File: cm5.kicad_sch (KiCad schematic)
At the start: 0 parts

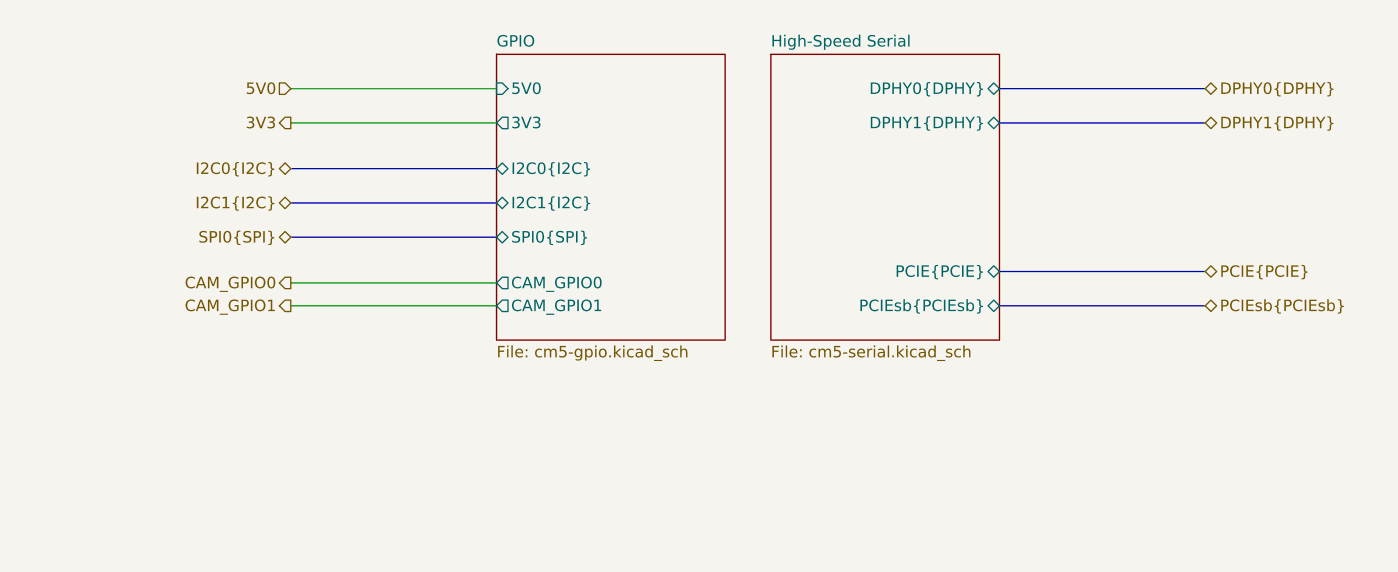
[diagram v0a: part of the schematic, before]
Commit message: prepared usb3, abstracted cameras, backplane connector
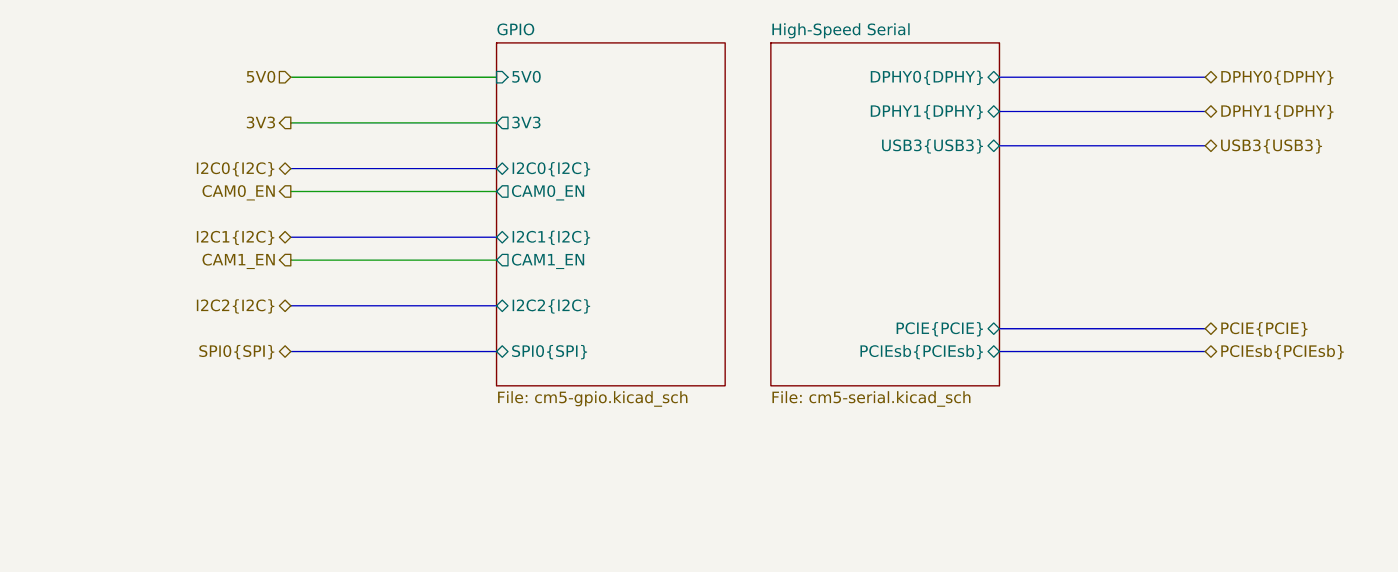
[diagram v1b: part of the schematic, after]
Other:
- sheet GPIO ports: added CAM0_EN, CAM1_EN, I2C2{I2C}; removed CAM_GPIO0, CAM_GPIO1
- sheet High-Speed Serial ports: added USB3{USB3}; removed none
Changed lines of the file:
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@@
 	(title_block
 		(title "CUTIE-CITRUS PCB")
-		(date "2025-11-24")
+		(date "2025-12-11")
 		(rev "A")
 		(company "Andre S Winkel | Highlander Space Program | University of California, Riverside")
@@
 	(bus
 		(pts
+			(xy 100.33 109.22) (xy 123.19 109.22)
+		)
+		(stroke
+			(width 0)
+			(type default)
+		)
+	)
+	(bus
+		(pts
+			(xy 179.07 109.22) (xy 201.93 109.22)
+		)
+		(stroke
+			(width 0)
+			(type default)
+		)
+	)
+	(bus
+		(pts
+			(xy 179.07 106.68) (xy 201.93 106.68)
+		)
+		(stroke
+			(width 0)
+			(type default)
+		)
+	)
+	(bus
+		(pts
+			(xy 100.33 88.9) (xy 123.19 88.9)
+		)
+		(stroke
+			(width 0)
+			(type default)
+		)
+	)
+	(bus
+		(pts
+			(xy 179.07 78.74) (xy 201.93 78.74)
+		)
+		(stroke
+			(width 0)
+			(type default)
+		)
+	)
+	(wire
+		(pts
+			(xy 100.33 83.82) (xy 123.19 83.82)
+		)
+		(stroke
+			(width 0.381)
+			(type default)
+			(color 255 153 0 1)
+		)
+	)
+	(wire
+		(pts
+			(xy 100.33 78.74) (xy 123.19 78.74)
+		)
+		(stroke
+			(width 0.508)
+			(type default)
+			(color 255 0 0 1)
+		)
+	)
+	(wire
+		(pts
+			(xy 100.33 99.06) (xy 123.19 99.06)
+		)
+		(stroke
+			(width 0)
+			(type default)
+		)
+	)
+	(bus
+		(pts
+			(xy 179.07 86.36) (xy 201.93 86.36)
+		)
+		(stroke
+			(width 0)
+			(type default)
+		)
+	)
+	(bus
+		(pts
+			(xy 100.33 104.14) (xy 123.19 104.14)
+		)
+		(stroke
+			(width 0)
+			(type default)
+		)
+	)
+	(bus
+		(pts
 			(xy 100.33 96.52) (xy 123.19 96.52)
 		)
@@
 	(bus
 		(pts
-			(xy 179.07 104.14) (xy 201.93 104.14)
-		)
-		(stroke
-			(width 0)
-			(type default)
-		)
-	)
-	(bus
-		(pts
-			(xy 179.07 100.33) (xy 201.93 100.33)
-		)
-		(stroke
-			(width 0)
-			(type default)
-		)
-	)
-	(bus
-		(pts
-			(xy 100.33 88.9) (xy 123.19 88.9)
-		)
-		(stroke
-			(width 0)
-			(type default)
-		)
-	)
-	(bus
-		(pts
-			(xy 179.07 80.01) (xy 201.93 80.01)
+			(xy 179.07 82.55) (xy 201.93 82.55)
 		)
 		(stroke
@@
 	(wire
 		(pts
-			(xy 100.33 83.82) (xy 123.19 83.82)
-		)
-		(stroke
-			(width 0.381)
-			(type default)
-			(color 255 153 0 1)
-		)
-	)
-	(wire
-		(pts
-			(xy 100.33 80.01) (xy 123.19 80.01)
-		)
-		(stroke
-			(width 0.508)
-			(type default)
-			(color 255 0 0 1)
-		)
-	)
-	(wire
-		(pts
-			(xy 100.33 104.14) (xy 123.19 104.14)
-		)
-		(stroke
-			(width 0)
-			(type default)
-		)
-	)
-	(bus
-		(pts
-			(xy 100.33 92.71) (xy 123.19 92.71)
-		)
-		(stroke
-			(width 0)
-			(type default)
-		)
-	)
-	(bus
-		(pts
-			(xy 179.07 83.82) (xy 201.93 83.82)
-		)
-		(stroke
-			(width 0)
-			(type default)
-		)
-	)
-	(wire
-		(pts
-			(xy 100.33 101.6) (xy 123.19 101.6)
+			(xy 100.33 91.44) (xy 123.19 91.44)
 		)
 		(stroke
@@
 	(hierarchical_label "DPHY0{DPHY}"
 		(shape bidirectional)
-		(at 201.93 80.01 0)
+		(at 201.93 78.74 0)
 		(effects
 			(font
@@
 	(hierarchical_label "I2C1{I2C}"
 		(shape bidirectional)
-		(at 100.33 92.71 180)
+		(at 100.33 96.52 180)
 		(effects
 			(font
@@
 		)
 	)
-	(hierarchical_label "CAM_GPIO1"
+	(hierarchical_label "CAM1_EN"
 		(shape output)
-		(at 100.33 104.14 180)
-		(effects
-			(font
-				(size 1.27 1.27)
-			)
-			(justify right)
-		)
-	)
-	(hierarchical_label "CAM_GPIO0"
+		(at 100.33 99.06 180)
+		(effects
+			(font
+				(size 1.27 1.27)
+			)
+			(justify right)
+		)
+	)
+	(hierarchical_label "CAM0_EN"
 		(shape output)
-		(at 100.33 101.6 180)
+		(at 100.33 91.44 180)
 		(effects
 			(font
@@
 	(hierarchical_label "5V0"
 		(shape input)
-		(at 100.33 80.01 180)
+		(at 100.33 78.74 180)
 		(effects
 			(font
@@
 	(hierarchical_label "DPHY1{DPHY}"
 		(shape bidirectional)
-		(at 201.93 83.82 0)
+		(at 201.93 82.55 0)
 		(effects
 			(font
@@
 	(hierarchical_label "SPI0{SPI}"
 		(shape bidirectional)
-		(at 100.33 96.52 180)
+		(at 100.33 109.22 180)
 		(effects
 			(font
@@
 	(hierarchical_label "PCIE{PCIE}"
 		(shape bidirectional)
-		(at 201.93 100.33 0)
+		(at 201.93 106.68 0)
 		(effects
 			(font
@@
 		)
 	)
+	(hierarchical_label "USB3{USB3}"
+		(shape bidirectional)
+		(at 201.93 86.36 0)
+		(effects
+			(font
+				(size 1.27 1.27)
+			)
+			(justify left)
+		)
+	)
 	(hierarchical_label "PCIEsb{PCIEsb}"
 		(shape bidirectional)
-		(at 201.93 104.14 0)
+		(at 201.93 109.22 0)
 		(effects
 			(font
@@
 		)
 	)
+	(hierarchical_label "I2C2{I2C}"
+		(shape bidirectional)
+		(at 100.33 104.14 180)
+		(effects
+			(font
+				(size 1.27 1.27)
+			)
+			(justify right)
+		)
+	)
 	(sheet
-		(at 123.19 76.2)
-		(size 25.4 31.75)
+		(at 123.19 74.93)
+		(size 25.4 38.1)
 		(exclude_from_sim no)
 		(in_bom yes)
@@
 		)
 		(property "Sheetname" "GPIO"
-			(at 123.19 75.4884 0)
+			(at 123.19 74.2184 0)
 			(effects
 				(font
@@
 		)
 		(property "Sheetfile" "cm5-gpio.kicad_sch"
-			(at 123.19 108.5346 0)
+			(at 123.19 113.6146 0)
 			(effects
 				(font
@@
 		)
 		(pin "5V0" input
-			(at 123.19 80.01 180)
-			(effects
-				(font
-					(size 1.27 1.27)
-				)
-				(justify left)
-			)
-		)
-		(pin "CAM_GPIO0" output
-			(at 123.19 101.6 180)
-			(effects
-				(font
-					(size 1.27 1.27)
-				)
-				(justify left)
-			)
-		)
-		(pin "CAM_GPIO1" output
-			(at 123.19 104.14 180)
+			(at 123.19 78.74 180)
+			(effects
+				(font
+					(size 1.27 1.27)
+				)
+				(justify left)
+			)
+		)
+		(pin "CAM0_EN" output
+			(at 123.19 91.44 180)
+			(effects
+				(font
+					(size 1.27 1.27)
+				)
+				(justify left)
+			)
+		)
+		(pin "CAM1_EN" output
+			(at 123.19 99.06 180)
 			(effects
 				(font
@@
 		)
 		(pin "I2C1{I2C}" bidirectional
-			(at 123.19 92.71 180)
+			(at 123.19 96.52 180)
 			(effects
 				(font
@@
 		)
 		(pin "SPI0{SPI}" bidirectional
-			(at 123.19 96.52 180)
+			(at 123.19 109.22 180)
+			(effects
+				(font
+					(size 1.27 1.27)
+				)
+				(justify left)
+			)
+		)
+		(pin "I2C2{I2C}" bidirectional
+			(at 123.19 104.14 180)
 			(effects
 				(font
@@
 	)
 	(sheet
-		(at 153.67 76.2)
-		(size 25.4 31.75)
+		(at 153.67 74.93)
+		(size 25.4 38.1)
 		(exclude_from_sim no)
 		(in_bom yes)
@@
 		)
 		(property "Sheetname" "High-Speed Serial"
-			(at 153.67 75.4884 0)
+			(at 153.67 74.2184 0)
 			(effects
 				(font
@@
 		)
 		(property "Sheetfile" "cm5-serial.kicad_sch"
-			(at 153.67 108.5346 0)
+			(at 153.67 113.6146 0)
 			(effects
 				(font
@@
 		)
 		(pin "DPHY0{DPHY}" bidirectional
-			(at 179.07 80.01 0)
+			(at 179.07 78.74 0)
 			(effects
 				(font
@@
 		)
 		(pin "DPHY1{DPHY}" bidirectional
-			(at 179.07 83.82 0)
+			(at 179.07 82.55 0)
 			(effects
 				(font
@@
 		)
 		(pin "PCIE{PCIE}" bidirectional
-			(at 179.07 100.33 0)
+			(at 179.07 106.68 0)
 			(effects
 				(font
@@
 		)
 		(pin "PCIEsb{PCIEsb}" bidirectional
-			(at 179.07 104.14 0)
-			(effects
-				(font
+			(at 179.07 109.22 0)
+			(effects
+				(font
+					(size 1.27 1.27)
+				)
+				(justify right)
+			)
+		)
+		(pin "USB3{USB3}" bidirectional
+			(at 179.07 86.36 0)
+			(effects
+				(font

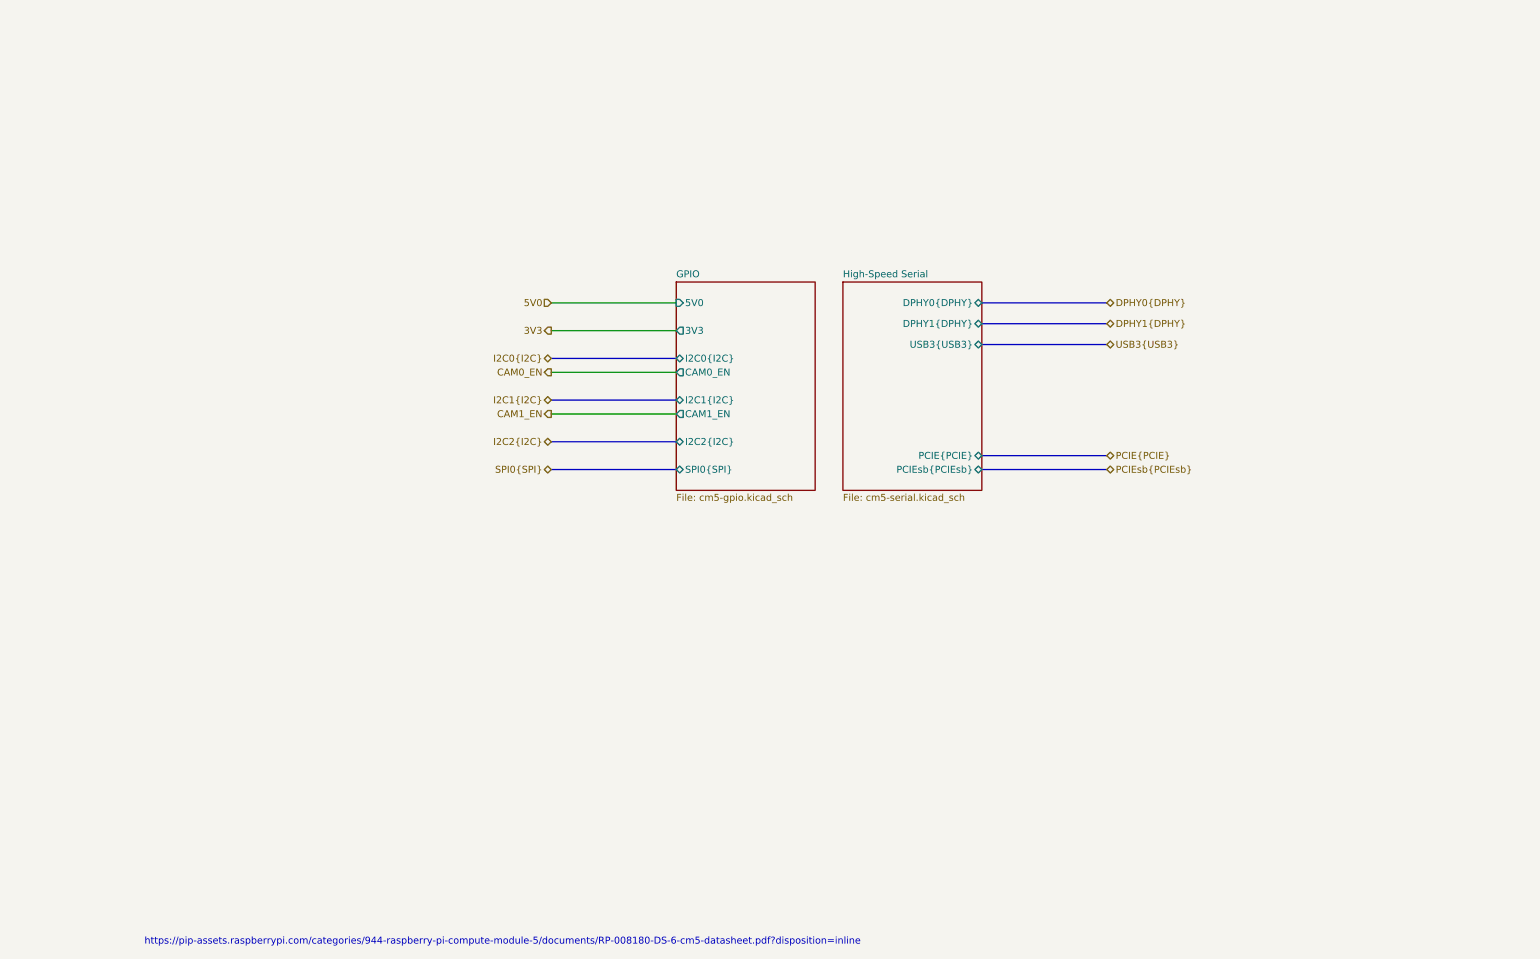
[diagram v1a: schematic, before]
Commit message: moved TPs
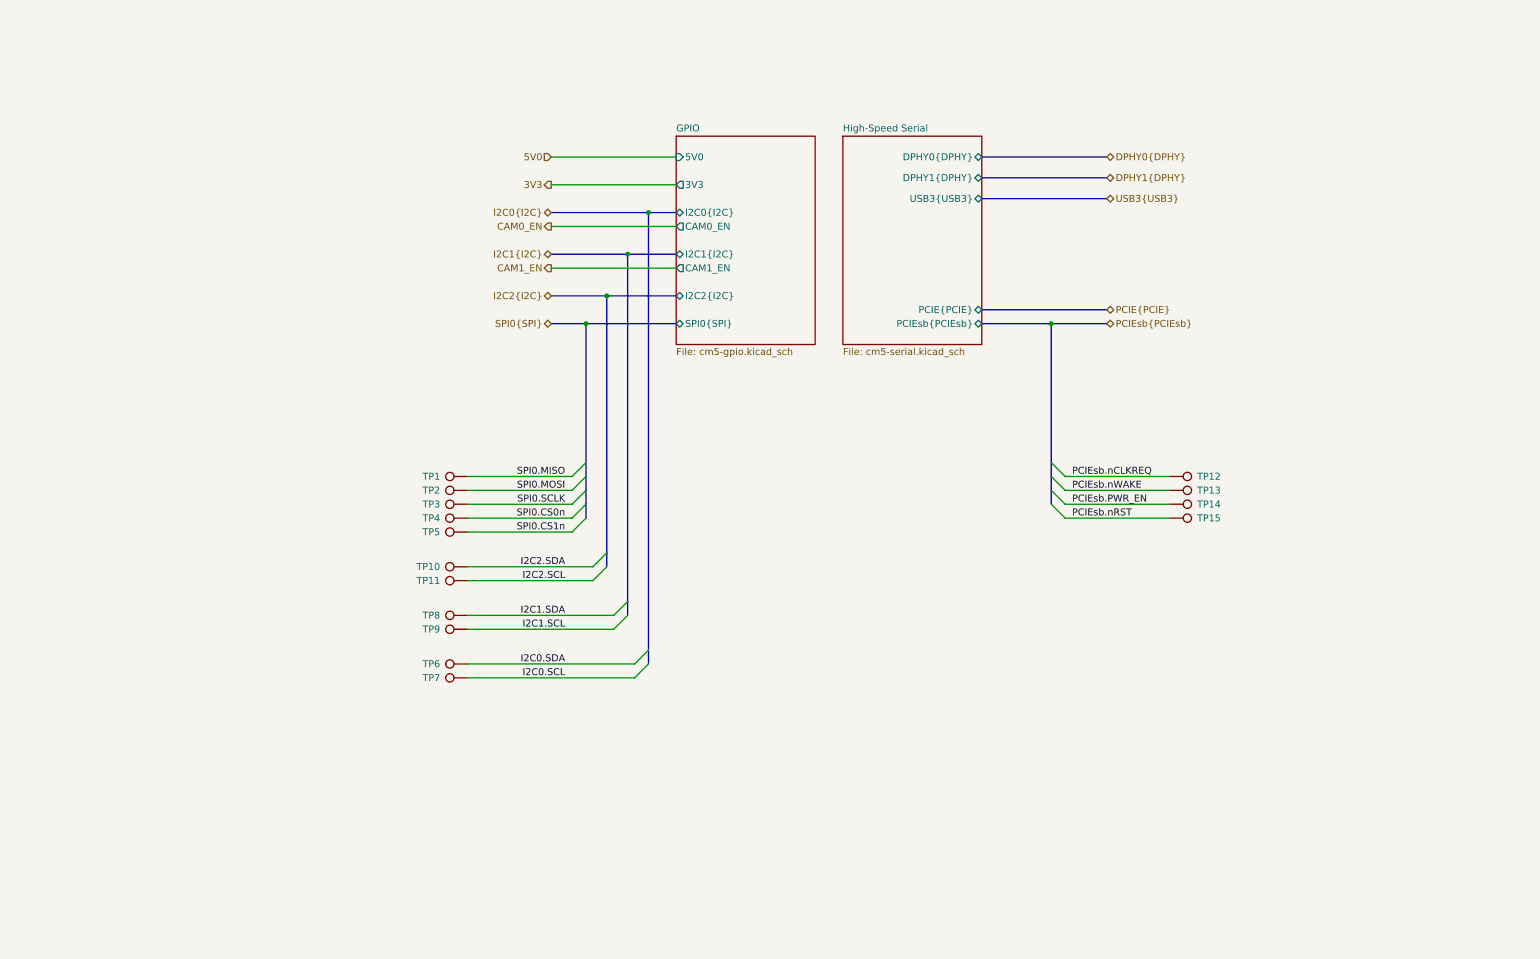
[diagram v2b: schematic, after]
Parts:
- added TP1, TP10, TP11, TP12, TP13, TP14, TP15, TP2, TP3, TP4, TP5, TP6, TP7, TP8, TP9: TestPoint, TestPoint:TestPoint_Pad_D1.0mm, symbol Connector:TestPoint
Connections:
- new net I2C0.SCL: TP7.1
- new net I2C0.SDA: TP6.1
- new net I2C1.SCL: TP9.1
- new net I2C1.SDA: TP8.1
- new net I2C2.SCL: TP11.1
- new net I2C2.SDA: TP10.1
- new net PCIEsb.PWR_EN: TP14.1
- new net PCIEsb.nCLKREQ: TP12.1
- new net PCIEsb.nRST: TP15.1
- new net PCIEsb.nWAKE: TP13.1
- new net SPI0.CS0n: TP4.1
- new net SPI0.CS1n: TP5.1
- new net SPI0.MISO: TP1.1
- new net SPI0.MOSI: TP2.1
- new net SPI0.SCLK: TP3.1
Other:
- note removed: "https://pip-assets.raspberrypi.com/categories/944-raspberry-pi-compute-module-5/documents/RP-008180-DS-6-cm5-datasheet.pdf?disposition=inline"

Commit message: moved power TPs to cm5 sheet
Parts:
- added 3V3, 5V0: TestPoint, TestPoint:TestPoint_Pad_D2.0mm, symbol library:TestPoint
- added GND1, GND2, GND3, GND4, GND5: TestPoint, TestPoint:TestPoint_Pad_D1.0mm, symbol library:TestPoint
- TP1, TP10, TP11, TP12, TP13, TP14, TP15, TP2, TP3, TP4, TP5, TP6, TP7, TP8, TP9: symbol Connector:TestPoint -> library:TestPoint
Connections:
- net 3V3: now also 3V3.1
- net 5V0: now also 5V0.1
- new net GND: GND1.1, GND2.1, GND3.1, GND4.1, GND5.1
